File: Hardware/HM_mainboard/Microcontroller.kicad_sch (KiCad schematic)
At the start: 17 parts, among them J2 USB4105-GF-A, J7 Conn_01x04, U3 ESP32-S3-WROOM-1, Y1 32.768 kHz

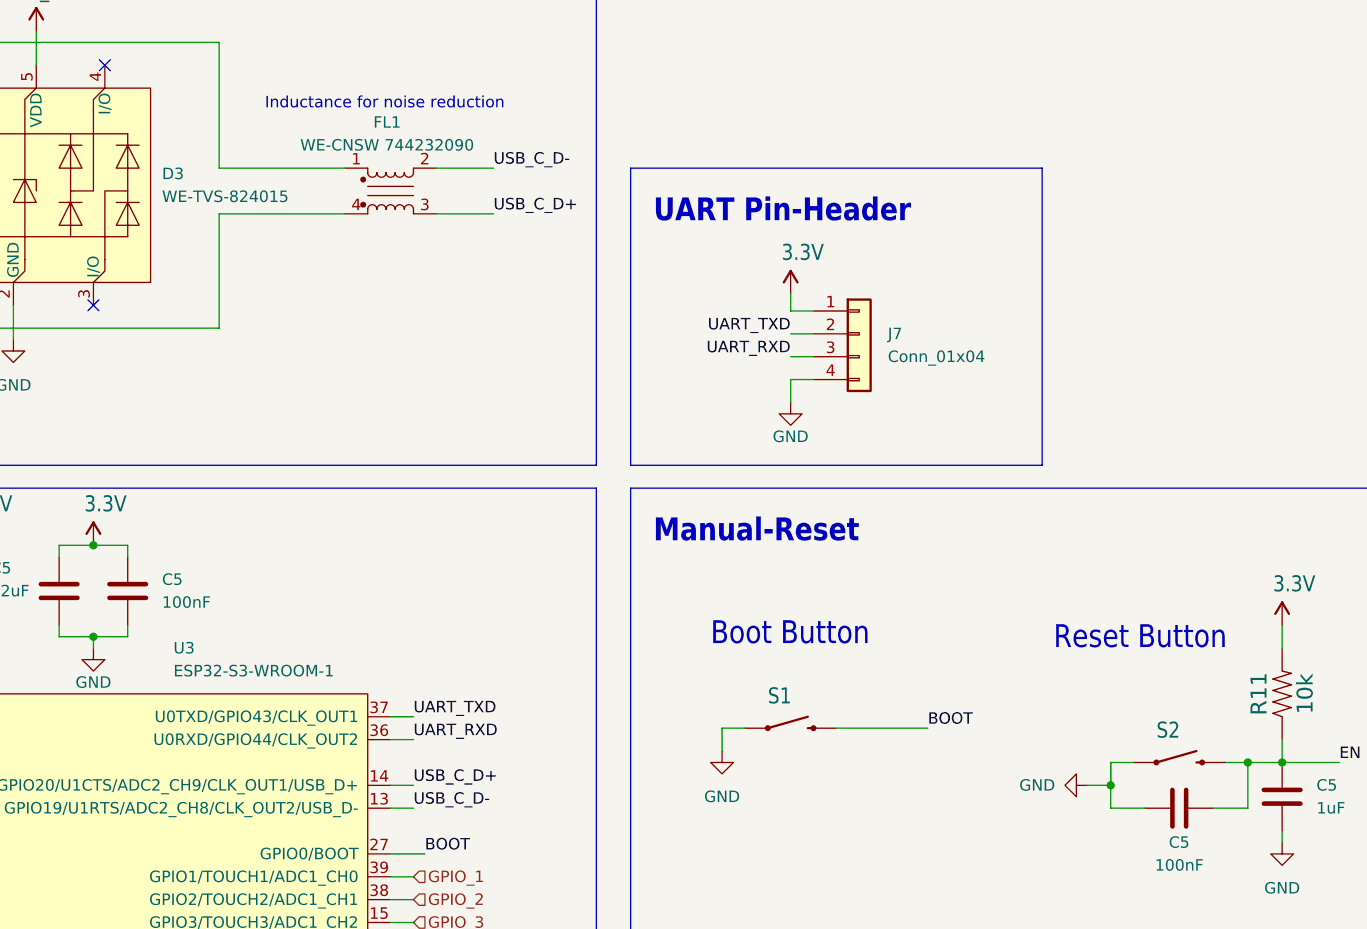
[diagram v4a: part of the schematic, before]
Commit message: Started component placement for PCB
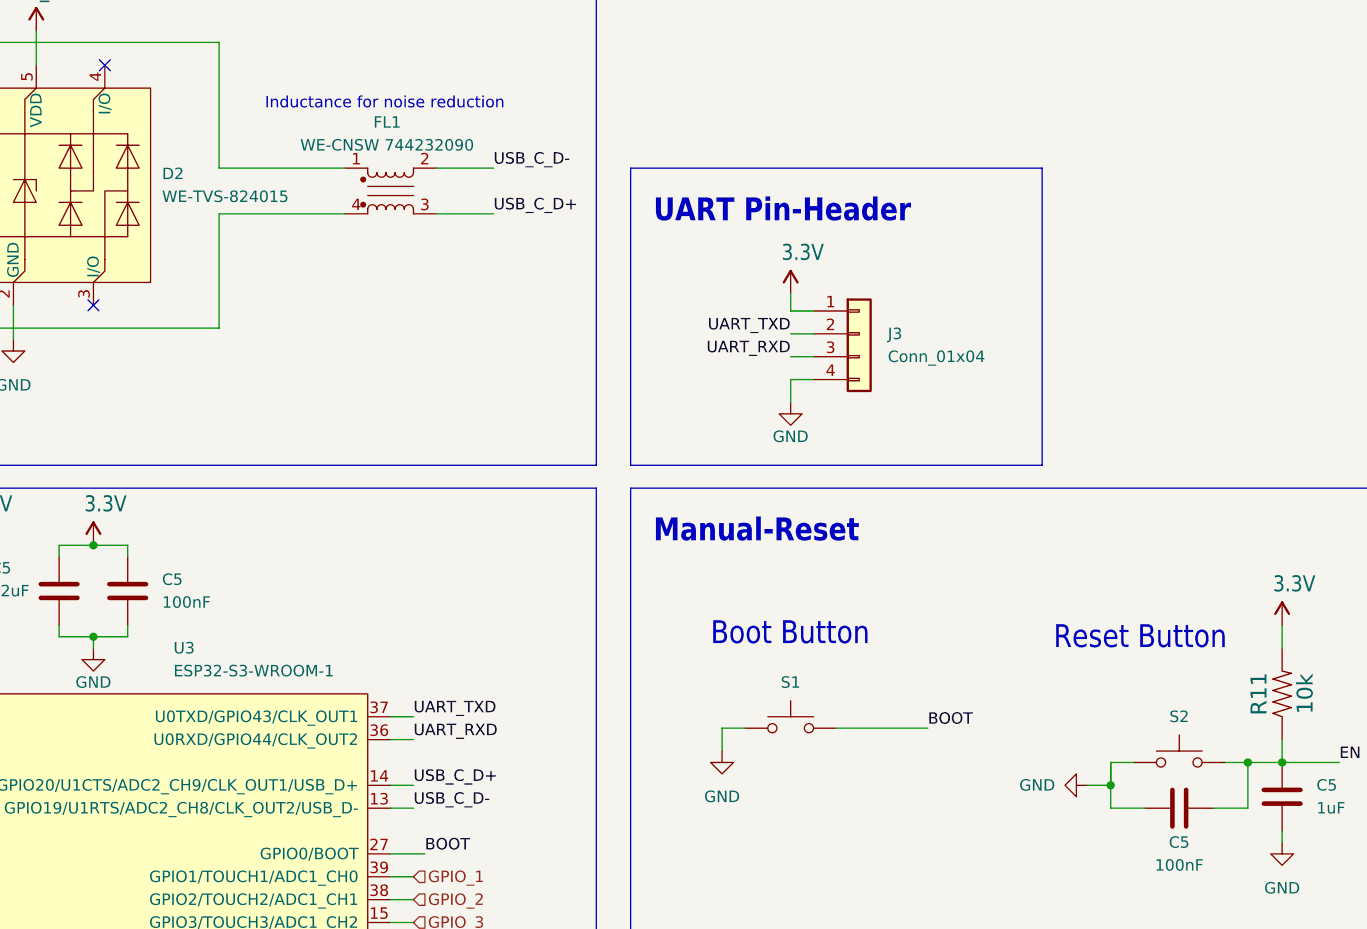
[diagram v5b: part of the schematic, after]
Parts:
- removed S1, S2: Push Button, Button_Switch_SMD:SW_Push_1P1T_NO_6x6mm_H9.5mm, symbol esp32-thing-eagle-import:SWITCH-MOMENTARY-2SMD-4.6X2.8MM
- added S1, S2: SW_Push, Button_Switch_SMD:SW_Push_1P1T_NO_6x6mm_H9.5mm, symbol Switch:SW_Push
- J3: renamed from J7; footprint (none) -> Connector_PinHeader_2.54mm:PinHeader_1x04_P2.54mm_Vertical
- renumbered D3 to D2
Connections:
- net BOOT: now also S1.2
- net EN: now also S2.2
- net GND: now also S1.1, S2.1
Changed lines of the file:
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@@
         )
         (path "/54a6df43-5475-46a2-9916-8b0260700d4c/8a725ce3-408a-4762-9df2-b56094186e56"
-          (reference "C15") (unit 1)
+          (reference "C8") (unit 1)
         )
       )
@@
         )
         (path "/54a6df43-5475-46a2-9916-8b0260700d4c/8a725ce3-408a-4762-9df2-b56094186e56"
-          (reference "C16") (unit 1)
+          (reference "C9") (unit 1)
         )
       )
@@
         )
         (path "/54a6df43-5475-46a2-9916-8b0260700d4c/8a725ce3-408a-4762-9df2-b56094186e56"
-          (reference "#PWR037") (unit 1)
+          (reference "#PWR015") (unit 1)
         )
         (path "/54a6df43-5475-46a2-9916-8b0260700d4c/9043a365-e24a-41b8-9f6d-decb4da0da6a"
@@
         )
         (path "/54a6df43-5475-46a2-9916-8b0260700d4c/8a725ce3-408a-4762-9df2-b56094186e56"
-          (reference "#PWR015") (unit 1)
+          (reference "#PWR016") (unit 1)
         )
         (path "/54a6df43-5475-46a2-9916-8b0260700d4c/9043a365-e24a-41b8-9f6d-decb4da0da6a"
@@
   (symbol (lib_id "usePAT:WE-TVS-824015") (at 110.49 50.8 0) (unit 1)
     (in_bom yes) (on_board yes) (dnp no) (fields_autoplaced)
-    (property "Reference" "D3" (at 125.73 48.8949 0)
+    (property "Reference" "D2" (at 125.73 48.8949 0)
       (effects (font (size 1.27 1.27)) (justify left))
     )
@@
       (project "HM_mainboard"
         (path "/54a6df43-5475-46a2-9916-8b0260700d4c/8a725ce3-408a-4762-9df2-b56094186e56"
-          (reference "D3") (unit 1)
+          (reference "D2") (unit 1)
         )
       )
@@
         )
         (path "/54a6df43-5475-46a2-9916-8b0260700d4c/8a725ce3-408a-4762-9df2-b56094186e56"
-          (reference "C14") (unit 1)
-        )
-      )
-    )
-  )
-  (symbol (lib_id "esp32-thing-eagle-import:SWITCH-MOMENTARY-2SMD-4.6X2.8MM") (at 195.58 110.49 0) (unit 1)
-    (in_bom yes) (on_board yes) (dnp no)
-    (property "Reference" "S1" (at 193.04 107.95 0)
-      (effects (font (size 1.778 1.5113)) (justify left bottom))
-    )
-    (property "Value" "Push Button" (at 193.04 113.03 0)
-      (effects (font (size 1.778 1.5113)) (justify left bottom) hide)
-    )
-    (property "Footprint" "Button_Switch_SMD:SW_Push_1P1T_NO_6x6mm_H9.5mm" (at 195.58 110.49 0)
-      (effects (font (size 1.27 1.27)) hide)
-    )
-    (property "Datasheet" "https://www.mouser.at/datasheet/2/358/typ_6x6_mm_tact_switches-1275689.pdf" (at 195.58 110.49 0)
-      (effects (font (size 1.27 1.27)) hide)
-    )
-    (pin "1")
-    (pin "2")
-    (pin "3")
-    (pin "4")
-    (instances
-      (project "HM_mainboard"
-        (path "/54a6df43-5475-46a2-9916-8b0260700d4c"
-          (reference "S1") (unit 1)
-        )
-        (path "/54a6df43-5475-46a2-9916-8b0260700d4c/8a725ce3-408a-4762-9df2-b56094186e56"
-          (reference "S1") (unit 1)
-        )
-      )
-      (project "esp32-thing"
-        (path "/8d063d86-d05a-414e-91f4-3532d6707197"
-          (reference "S2") (unit 1)
+          (reference "C7") (unit 1)
         )
       )
@@
         )
         (path "/54a6df43-5475-46a2-9916-8b0260700d4c/8a725ce3-408a-4762-9df2-b56094186e56"
-          (reference "#PWR038") (unit 1)
+          (reference "#PWR017") (unit 1)
         )
         (path "/54a6df43-5475-46a2-9916-8b0260700d4c/9043a365-e24a-41b8-9f6d-decb4da0da6a"
@@
         )
         (path "/54a6df43-5475-46a2-9916-8b0260700d4c/8a725ce3-408a-4762-9df2-b56094186e56"
-          (reference "#PWR016") (unit 1)
+          (reference "#PWR018") (unit 1)
         )
         (path "/54a6df43-5475-46a2-9916-8b0260700d4c/9043a365-e24a-41b8-9f6d-decb4da0da6a"
@@
         )
         (path "/54a6df43-5475-46a2-9916-8b0260700d4c/8a725ce3-408a-4762-9df2-b56094186e56"
-          (reference "R8") (unit 1)
+          (reference "R7") (unit 1)
         )
       )
@@
         )
         (path "/54a6df43-5475-46a2-9916-8b0260700d4c/8a725ce3-408a-4762-9df2-b56094186e56"
-          (reference "#SUPPLY023") (unit 1)
+          (reference "#SUPPLY012") (unit 1)
         )
       )
@@
         )
         (path "/54a6df43-5475-46a2-9916-8b0260700d4c/8a725ce3-408a-4762-9df2-b56094186e56"
-          (reference "#PWR032") (unit 1)
+          (reference "#PWR019") (unit 1)
         )
         (path "/54a6df43-5475-46a2-9916-8b0260700d4c/9043a365-e24a-41b8-9f6d-decb4da0da6a"
@@
         )
         (path "/54a6df43-5475-46a2-9916-8b0260700d4c/8a725ce3-408a-4762-9df2-b56094186e56"
-          (reference "C13") (unit 1)
+          (reference "C10") (unit 1)
         )
       )
@@
   (symbol (lib_id "Connector_Generic:Conn_01x04") (at 203.2 66.675 0) (unit 1)
     (in_bom yes) (on_board yes) (dnp no) (fields_autoplaced)
-    (property "Reference" "J7" (at 206.375 66.675 0)
+    (property "Reference" "J3" (at 206.375 66.675 0)
       (effects (font (size 1.27 1.27)) (justify left))
     )
@@
       (effects (font (size 1.27 1.27)) (justify left))
     )
-    (property "Footprint" "" (at 203.2 66.675 0)
+    (property "Footprint" "Connector_PinHeader_2.54mm:PinHeader_1x04_P2.54mm_Vertical" (at 203.2 66.675 0)
       (effects (font (size 1.27 1.27)) hide)
     )
@@
       (project "HM_mainboard"
         (path "/54a6df43-5475-46a2-9916-8b0260700d4c/8a725ce3-408a-4762-9df2-b56094186e56"
-          (reference "J7") (unit 1)
+          (reference "J3") (unit 1)
         )
       )
@@
         (path "/54a6df43-5475-46a2-9916-8b0260700d4c/137c5701-d01e-40ce-919d-b371cfda41da"
           (reference "#PWR01") (unit 1)
-        )
-      )
-    )
-  )
-  (symbol (lib_id "esp32-thing-eagle-import:SWITCH-MOMENTARY-2SMD-4.6X2.8MM") (at 238.76 114.3 0) (unit 1)
-    (in_bom yes) (on_board yes) (dnp no)
-    (property "Reference" "S2" (at 236.22 111.76 0)
-      (effects (font (size 1.778 1.5113)) (justify left bottom))
-    )
-    (property "Value" "Push Button " (at 233.68 118.11 0)
-      (effects (font (size 1.778 1.5113)) (justify left bottom) hide)
-    )
-    (property "Footprint" "Button_Switch_SMD:SW_Push_1P1T_NO_6x6mm_H9.5mm" (at 238.76 114.3 0)
-      (effects (font (size 1.27 1.27)) hide)
-    )
-    (property "Datasheet" "https://www.mouser.at/datasheet/2/358/typ_6x6_mm_tact_switches-1275689.pdf" (at 238.76 114.3 0)
-      (effects (font (size 1.27 1.27)) hide)
-    )
-    (pin "1")
-    (pin "2")
-    (pin "3")
-    (pin "4")
-    (instances
-      (project "HM_mainboard"
-        (path "/54a6df43-5475-46a2-9916-8b0260700d4c"
-          (reference "S2") (unit 1)
-        )
-        (path "/54a6df43-5475-46a2-9916-8b0260700d4c/8a725ce3-408a-4762-9df2-b56094186e56"
-          (reference "S2") (unit 1)
-        )
-      )
-      (project "esp32-thing"
-        (path "/8d063d86-d05a-414e-91f4-3532d6707197"
-          (reference "S1") (unit 1)
         )
       )
@@
     )
   )
+  (symbol (lib_id "Switch:SW_Push") (at 238.76 114.3 0) (unit 1)
+    (in_bom yes) (on_board yes) (dnp no) (fields_autoplaced)
+    (property "Reference" "S2" (at 238.76 109.22 0)
+      (effects (font (size 1.27 1.27)))
+    )
+    (property "Value" "SW_Push" (at 238.76 109.22 0)
+      (effects (font (size 1.27 1.27)) hide)
+    )
+    (property "Footprint" "Button_Switch_SMD:SW_Push_1P1T_NO_6x6mm_H9.5mm" (at 238.76 109.22 0)
+      (effects (font (size 1.27 1.27)) hide)
+    )
+    (property "Datasheet" "https://www.mouser.at/datasheet/2/358/typ_6x6_mm_tact_switches-1275689.pdf" (at 238.76 109.22 0)
+      (effects (font (size 1.27 1.27)) hide)
+    )
+    (pin "1")
+    (pin "2")
+    (instances
+      (project "HM_mainboard"
+        (path "/54a6df43-5475-46a2-9916-8b0260700d4c/8a725ce3-408a-4762-9df2-b56094186e56"
+          (reference "S2") (unit 1)
+        )
+      )
+    )
+  )
   (symbol (lib_id "esp32-thing-eagle-import:3.3V") (at 250.19 99.06 0) (unit 1)
     (in_bom yes) (on_board yes) (dnp no)
@@
         )
         (path "/54a6df43-5475-46a2-9916-8b0260700d4c/8a725ce3-408a-4762-9df2-b56094186e56"
-          (reference "#SUPPLY012") (unit 1)
+          (reference "#SUPPLY013") (unit 1)
         )
       )
@@
         )
       )
+    )
+  )
+  (symbol (lib_id "Switch:SW_Push") (at 195.58 110.49 0) (unit 1)
+    (in_bom yes) (on_board yes) (dnp no) (fields_autoplaced)
+    (property "Reference" "S1" (at 195.58 105.41 0)
+      (effects (font (size 1.27 1.27)))
+    )
+    (property "Value" "SW_Push" (at 195.58 105.41 0)
+      (effects (font (size 1.27 1.27)) hide)
+    )
+    (property "Footprint" "Button_Switch_SMD:SW_Push_1P1T_NO_6x6mm_H9.5mm" (at 195.58 105.41 0)
+      (effects (font (size 1.27 1.27)) hide)
+    )
+    (property "Datasheet" "https://www.mouser.at/datasheet/2/358/typ_6x6_mm_tact_switches-1275689.pdf" (at 195.58 105.41 0)
+      (effects (font (size 1.27 1.27)) hide)
+    )
+    (pin "1")
+    (pin "2")
+    (instances
+      (project "HM_mainboard"
+        (path "/54a6df43-5475-46a2-9916-8b0260700d4c/8a725ce3-408a-4762-9df2-b56094186e56"
+          (reference "S1") (unit 1)
+        )
+      )
